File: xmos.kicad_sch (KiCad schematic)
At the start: 66 parts, among them Q1 LBSS138WT1G, Q2 BC847B, U10 SN74LVC125APWR, U7 XU316-1024-QF60B-C24, U8 W25Q128JVSIQ, U9 TLV73333PDBVR, Y2 24MHz

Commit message: routing update
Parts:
- removed R48, R49: 33R, Resistor_SMD:R_0402_1005Metric, symbol Device:R
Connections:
- net BUT_A: no longer names the net of U7.50 (X0D41)
- net XL_DN0: no longer names the net of U7.35 (X1D17)
- net XL_DN1: no longer names the net of U7.33 (X1D16)
- net XU316_WS2812: no longer names the net of U7.48 (X0D42)
- no-connect marks 1 -> 7

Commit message: routing update
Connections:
- net QSPI_D2: no longer U7.6 (X0D00)
- no-connect marks 7 -> 8
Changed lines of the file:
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@@
+	)
+	(no_connect
+		(at 52.07 48.26)
 	)
 	(no_connect
@@
 	(wire
 		(pts
-			(xy 29.21 48.26) (xy 52.07 48.26)
-		)
-		(stroke
-			(width 0)
-			(type default)
-		)
-	)
-	(wire
-		(pts
 			(xy 193.04 200.66) (xy 209.55 200.66)
 		)
@@
 		)
 	)
-	(label "QSPI_D2"
-		(at 29.21 48.26 0)
-		(effects
-			(font
-				(size 1.27 1.27)
-			)
-			(justify left bottom)
-		)
-	)

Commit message: final touches
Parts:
- D3, D4, D5, D6, D7, D8: value PESD0402-050 -> PESD0402V05
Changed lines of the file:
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@@
 			)
 		)
-		(property "Value" "PESD0402-050"
+		(property "Value" "PESD0402V05"
 			(at 195.58 180.3399 90)
 			(effects
@@
 			)
 		)
-		(property "Description" "PESD0402-050, 5V TVS, 0.3pF"
+		(property "Description" "PESD0402V05, 5V TVS, 0.3pF"
 			(at 193.04 179.07 0)
 			(effects
@@
 			)
 		)
-		(property "Value" "PESD0402-050"
+		(property "Value" "PESD0402V05"
 			(at 242.57 199.644 90)
 			(effects
@@
 			)
 		)
-		(property "Description" "PESD0402-050, 5V TVS, 0.3pF"
+		(property "Description" "PESD0402V05, 5V TVS, 0.3pF"
 			(at 250.19 204.47 0)
 			(effects
@@
 			)
 		)
-		(property "Value" "PESD0402-050"
+		(property "Value" "PESD0402V05"
 			(at 242.57 171.704 90)
 			(effects
@@
 			)
 		)
-		(property "Description" "PESD0402-050, 5V TVS, 0.3pF"
+		(property "Description" "PESD0402V05, 5V TVS, 0.3pF"
 			(at 250.19 176.53 0)
 			(effects
@@
 			)
 		)
-		(property "Value" "PESD0402-050"
+		(property "Value" "PESD0402V05"
 			(at 194.818 204.47 90)
 			(effects
@@
 			)
 		)
-		(property "Description" "PESD0402-050, 5V TVS, 0.3pF"
+		(property "Description" "PESD0402V05, 5V TVS, 0.3pF"
 			(at 193.04 204.47 0)
 			(effects
@@
 			)
 		)
-		(property "Value" "PESD0402-050"
+		(property "Value" "PESD0402V05"
 			(at 248.158 194.818 90)
 			(effects
@@
 			)
 		)
-		(property "Description" "PESD0402-050, 5V TVS, 0.3pF"
+		(property "Description" "PESD0402V05, 5V TVS, 0.3pF"
 			(at 259.08 199.39 0)
 			(effects
@@
 			)
 		)
-		(property "Value" "PESD0402-050"
+		(property "Value" "PESD0402V05"
 			(at 261.62 172.7199 90)
 			(effects
@@
 			)
 		)
-		(property "Description" "PESD0402-050, 5V TVS, 0.3pF"
+		(property "Description" "PESD0402V05, 5V TVS, 0.3pF"
 			(at 259.08 171.45 0)
 			(effects

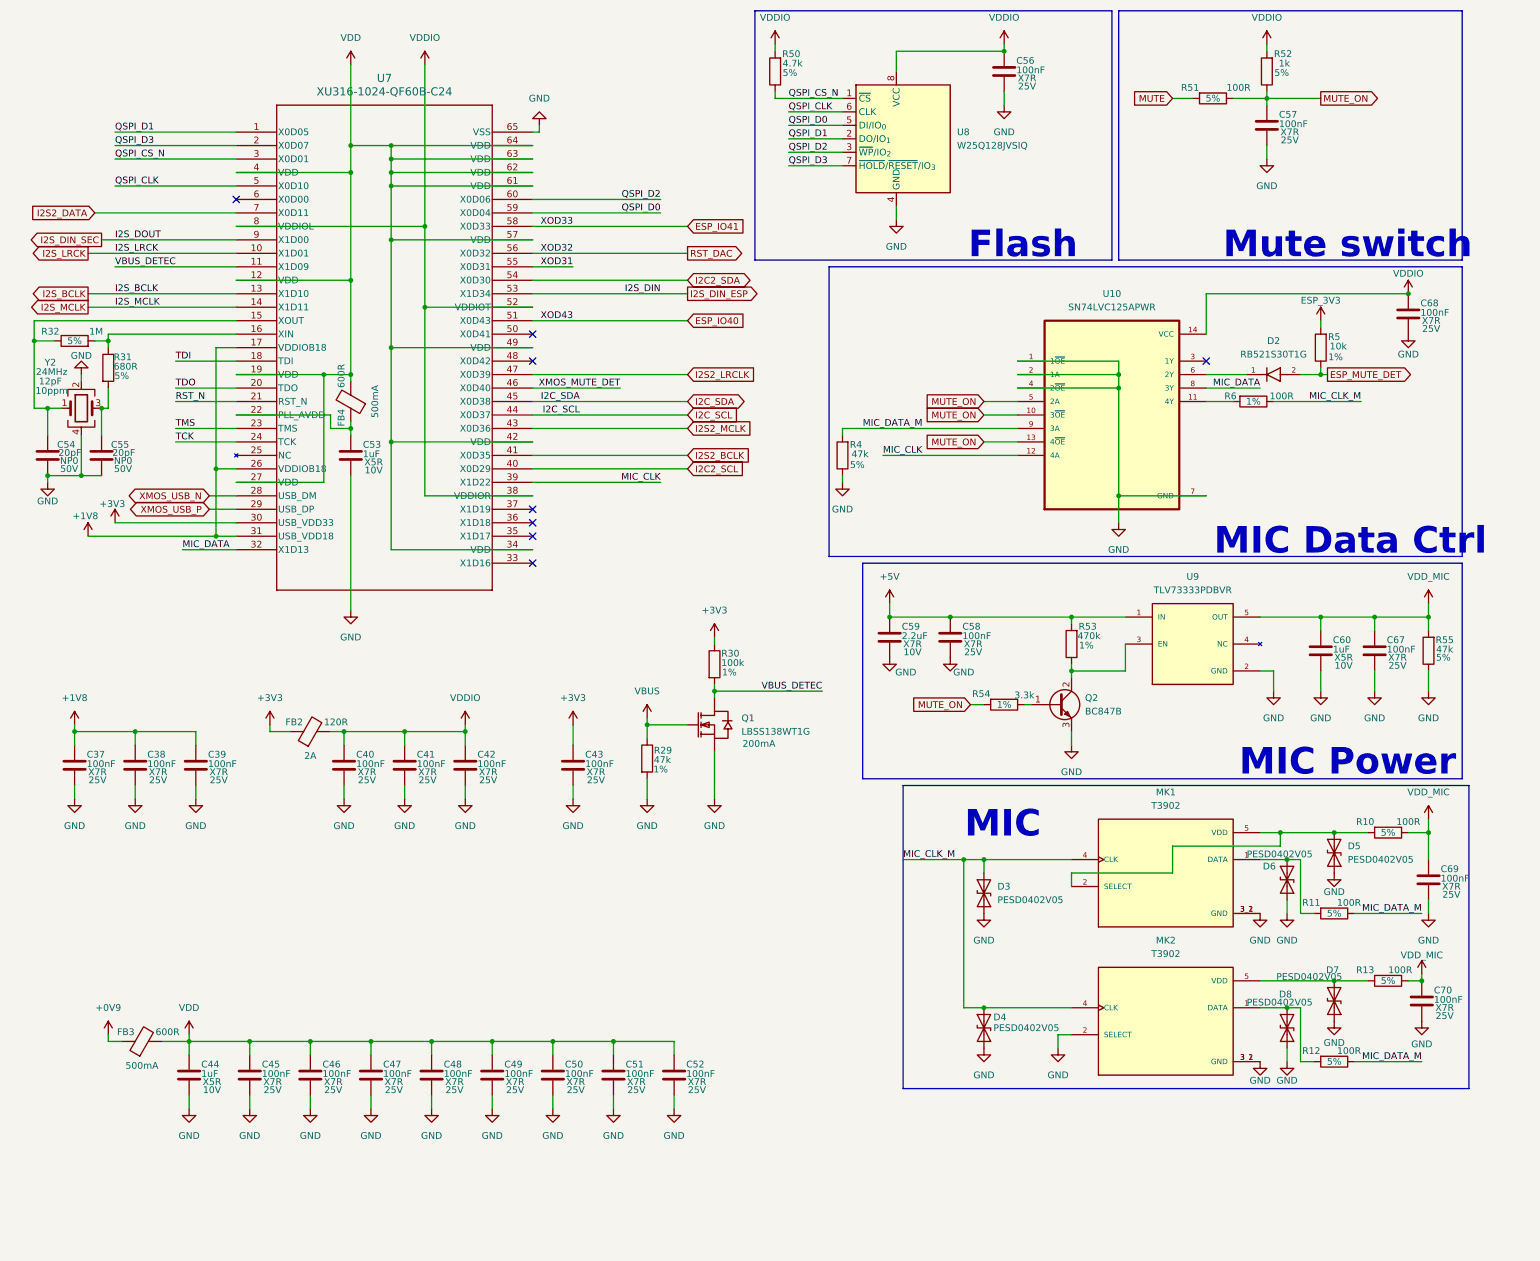
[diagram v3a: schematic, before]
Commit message: modifications for manufacturing
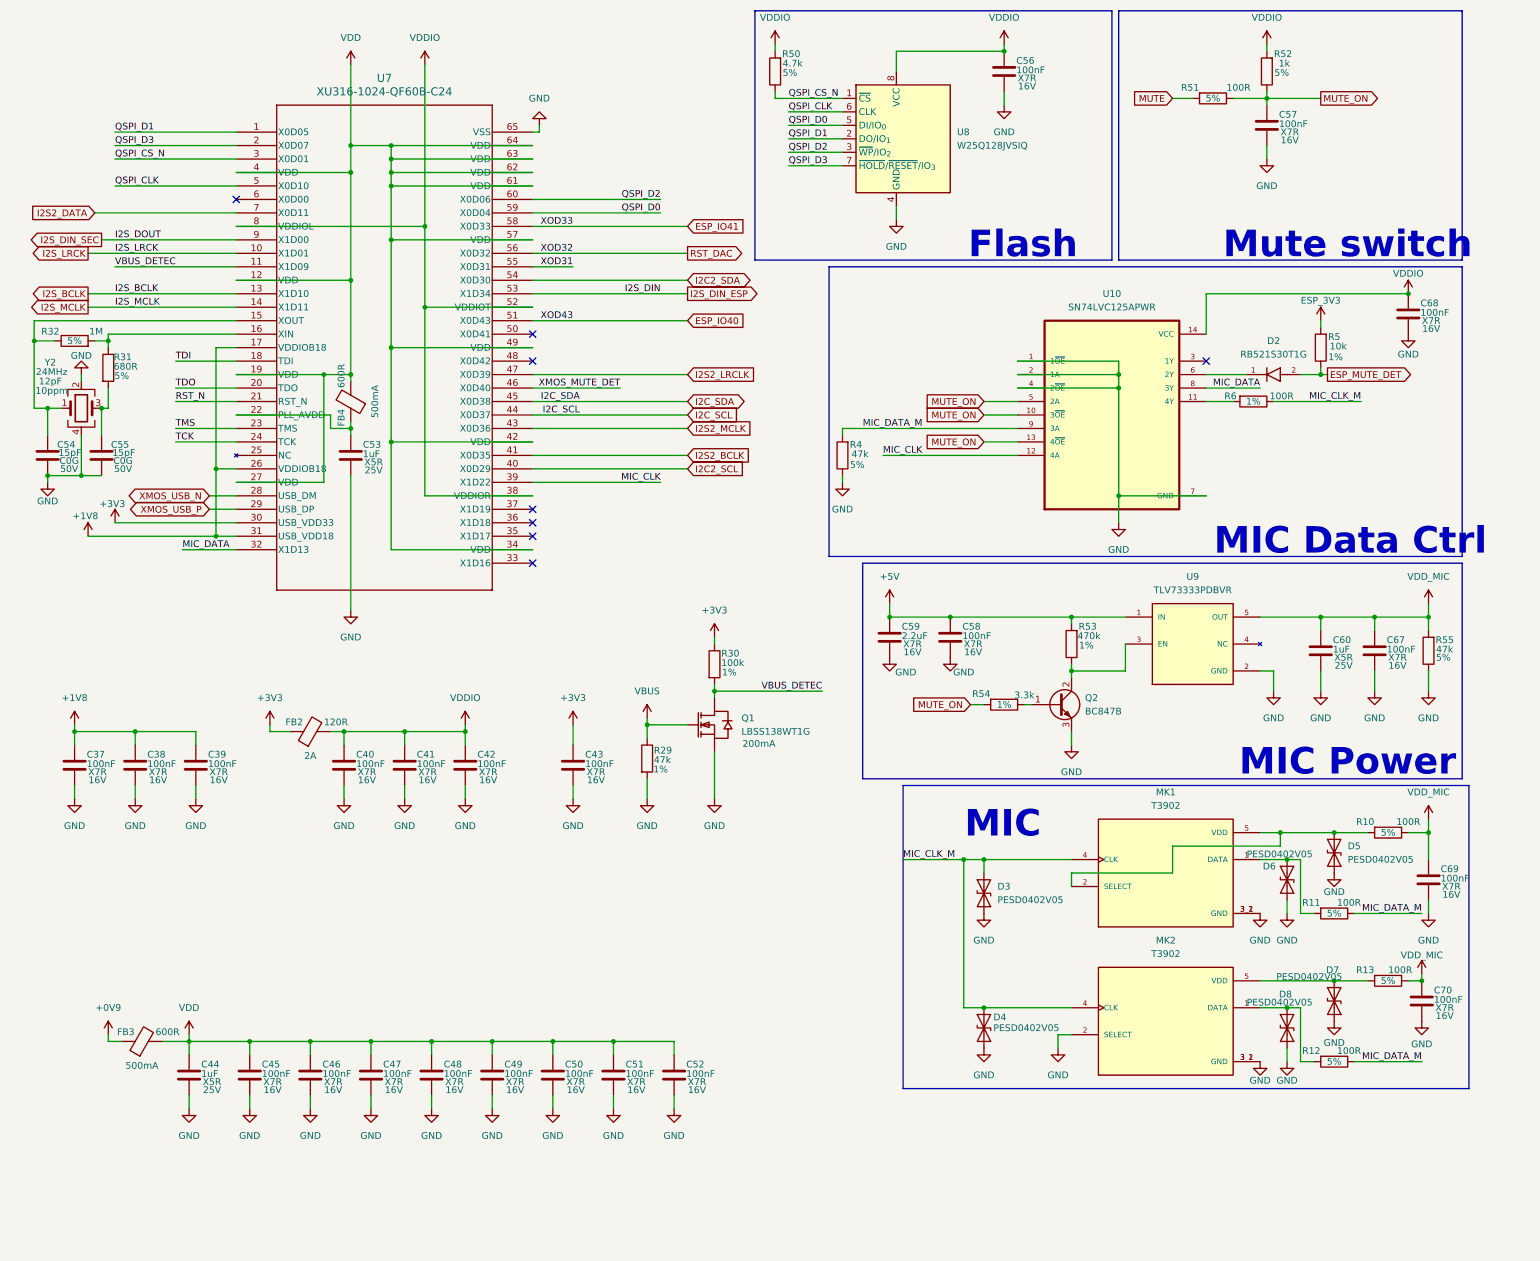
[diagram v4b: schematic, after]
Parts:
- C37, C38, C39, C40, C41, C42, C43, C45, C46, C47, C48, C49, C50, C51, C52, C56, C57, C58, C67, C68, C69, C70: Supplier Part (none) -> C1525; Voltage 25V -> 16V
- C44, C53, C60: Supplier Part (none) -> C52923; Voltage 10V -> 25V
- C54, C55: value 20pF -> 15pF; Dielectric NP0 -> C0G; Supplier Part (none) -> C1548
- C59: footprint Capacitor_SMD:C_0402_1005Metric -> Capacitor_SMD:C_0603_1608Metric; Voltage 10V -> 16V
- D2: Supplier Part (none) -> C27636108
- D3, D4, D5, D6, D7, D8: MANUFACTURER (none) -> DOWO; MP (none) -> PESD0402V05; Supplier Part (none) -> C19626254
- FB2: MANUFACTURER (none) -> Murata Electronics; MP (none) -> BLM18PG121SN1D; Supplier Part (none) -> C14709
- FB3, FB4: MANUFACTURER (none) -> Murata Electronics; MP (none) -> BLM18KG601SN1D; Part number BLM18AG601SN1D -> BLM18KG601SN1D; Supplier Part (none) -> C85833
- MK1, MK2: Supplier Part (none) -> C3171752
- Q1: MANUFACTURER (none) -> LRC; MP (none) -> LBSS138WT1G
- Q2: MANUFACTURER (none) -> hongjiacheng; MP (none) -> BC847B; Supplier Part (none) -> C20069135
- R10, R11, R12, R13, R51, R6: Supplier Part (none) -> C25076
- R29, R4, R55: Supplier Part (none) -> C25792
- R30: Supplier Part (none) -> C25530
- R31: Supplier Part (none) -> C25130
- R32: Supplier Part (none) -> C26083
- R5: Supplier Part (none) -> C25744
- R50: Supplier Part (none) -> C25900
- R52: Supplier Part (none) -> C11702
- R53: Supplier Part (none) -> C25790
- R54: Supplier Part (none) -> C25890
- U10: MANUFACTURER (none) -> Texas Instruments; Supplier Part (none) -> C7813
- U7: MANUFACTURER (none) -> XMOS; MP (none) -> XU316-1024-QF60B-C24; Supplier Part (none) -> C6617472
- U8: MANUFACTURER (none) -> Winbond Elec; MP (none) -> W25Q128JVSIQ; Supplier Part (none) -> C97521
- U9: Supplier Part (none) -> C134139
- Y2: MANUFACTURER (none) -> YXC Crystal Oscillators; MP (none) -> X322524MOB4SI; Manufacturer (none) -> YXC Crystal Oscillators; Supplier Part (none) -> C70590

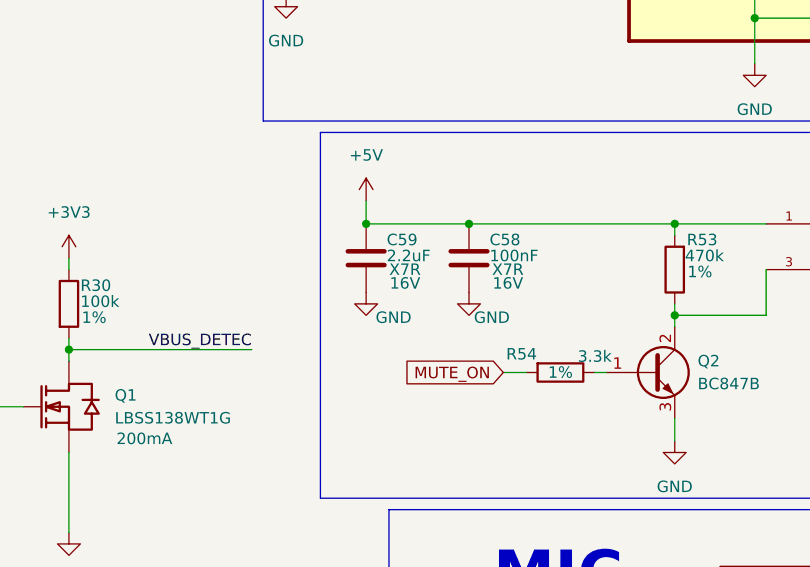
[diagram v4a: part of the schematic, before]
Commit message: modifications for manufacturing
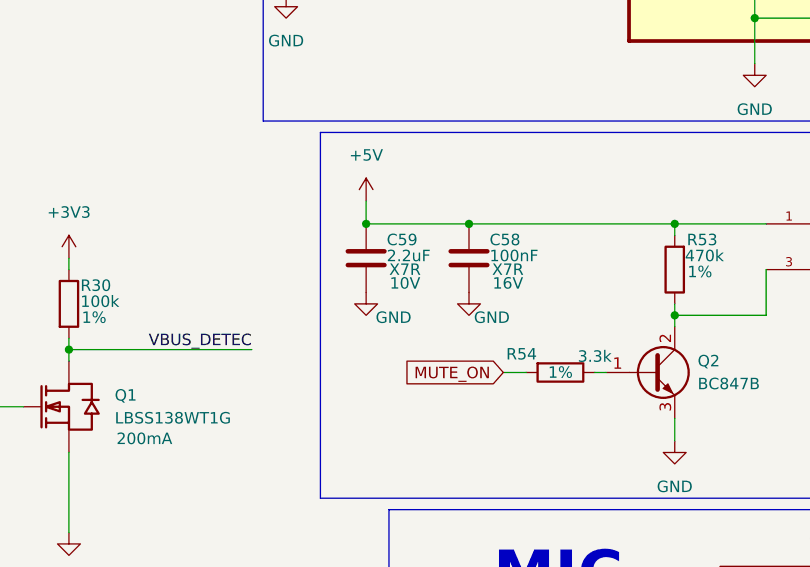
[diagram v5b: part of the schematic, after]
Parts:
- C59: Supplier Part (none) -> C86018; Voltage 16V -> 10V
- D2: Manufacturer (none) -> ON SEMICONDUCTOR; Manufacturer Part (none) -> RB521S30T1G
- D3, D4, D5, D6, D7, D8: Manufacturer (none) -> DOWO; Manufacturer Part (none) -> PESD0402V05
- FB2: Manufacturer Part (none) -> BLM18PG121SN1D
- FB3, FB4: Manufacturer Part (none) -> BLM18KG601SN1D
- MK1, MK2: Manufacturer (none) -> TDK InvenSense; Manufacturer Part (none) -> T3902
- Q2: Manufacturer (none) -> hongjiacheng; Manufacturer Part (none) -> BC847B
- U10: Manufacturer (none) -> Texas Instruments; Manufacturer Part (none) -> SN74LVC125APWR
- U7: Manufacturer (none) -> XMOS; Manufacturer Part (none) -> XU316-1024-QF60B-C24
- U8: Manufacturer (none) -> Winbond Elec; Manufacturer Part (none) -> W25Q128JVSIQ
- U9: Manufacturer (none) -> Texas Instruments; Manufacturer Part (none) -> TLV73333PDBVR
- Y2: Manufacturer Part (none) -> X322524MOB4SI

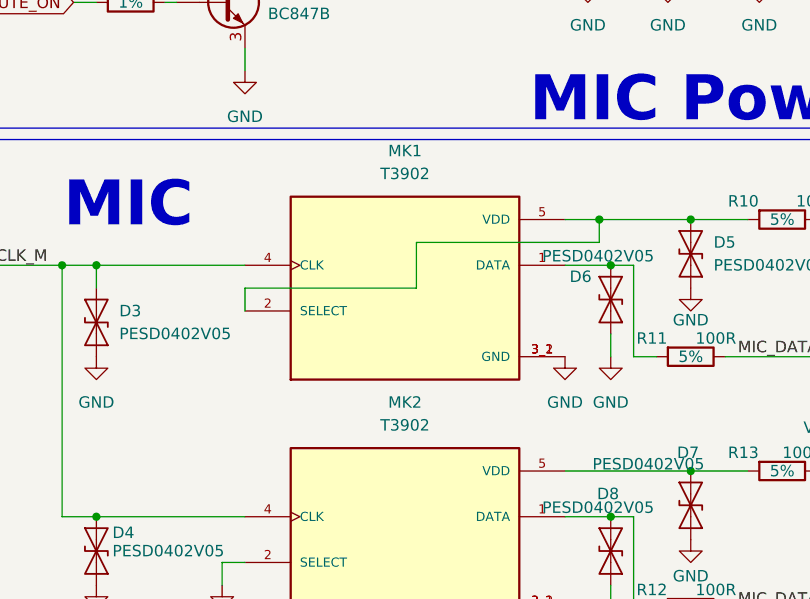
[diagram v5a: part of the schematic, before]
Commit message: modifications for manufacturing
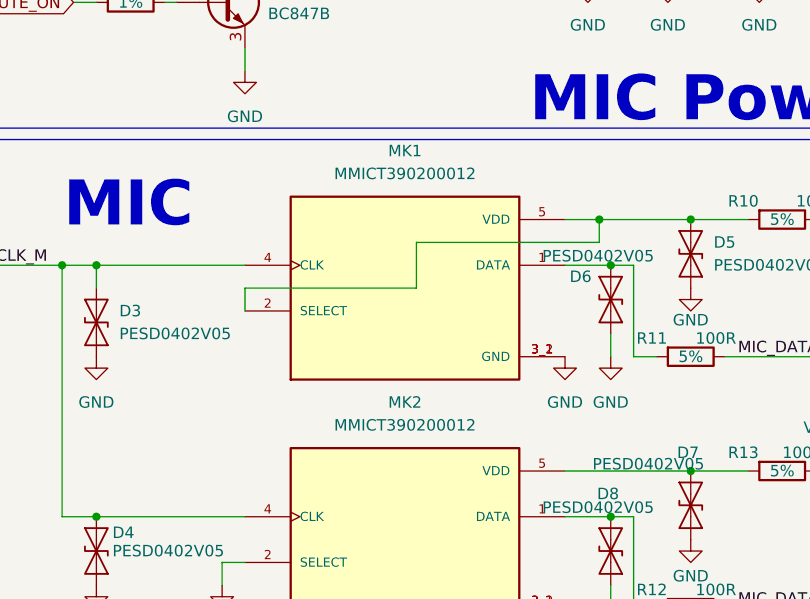
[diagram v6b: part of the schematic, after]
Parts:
- C37, C38, C39, C40, C41, C42, C43, C45, C46, C47, C48, C49, C50, C51, C52, C56, C57, C58, C67, C68, C69, C70: Manufacturer (none) -> Samsung Electro-Mechanics; Manufacturer Part (none) -> CL05B104KO5NNNC
- C44, C53, C60: Manufacturer (none) -> Samsung Electro-Mechanics; Manufacturer Part (none) -> CL05A105KA5NQNC
- C54, C55: Manufacturer (none) -> FH (Guangdong Fenghua Advanced Tech); Manufacturer Part (none) -> 0402CG150J500NT
- C59: Manufacturer (none) -> Murata Electronics; Manufacturer Part (none) -> GRM188R71A225KE15D
- MK1, MK2: value T3902 -> MMICT390200012; Manufacturer Part T3902 -> MMICT390200012
- R10, R11, R12, R13, R51, R6: Manufacturer (none) -> UNI-ROYAL(Uniroyal Elec); Manufacturer Part (none) -> 0402WGF1000TCE
- R29, R4, R55: Manufacturer (none) -> UNI-ROYAL(Uniroyal Elec); Manufacturer Part (none) -> 0402WGF4702TCE
- R30: Manufacturer (none) -> UNI-ROYAL(Uniroyal Elec); Manufacturer Part (none) -> 0402WGJ0104TCE
- R31: Manufacturer (none) -> UNI-ROYAL(Uniroyal Elec); Manufacturer Part (none) -> 0402WGF6800TCE
- R32: Manufacturer (none) -> UNI-ROYAL(Uniroyal Elec); Manufacturer Part (none) -> 0402WGF1004TCE
- R5: Manufacturer (none) -> UNI-ROYAL(Uniroyal Elec); Manufacturer Part (none) -> 0402WGF1002TCE
- R50: Manufacturer (none) -> UNI-ROYAL(Uniroyal Elec); Manufacturer Part (none) -> 0402WGF4701TCE
- R52: Manufacturer (none) -> UNI-ROYAL(Uniroyal Elec); Manufacturer Part (none) -> 0402WGF1001TCE
- R53: Manufacturer (none) -> UNI-ROYAL(Uniroyal Elec); Manufacturer Part (none) -> 0402WGF4703TCE
- R54: Manufacturer (none) -> UNI-ROYAL(Uniroyal Elec); Manufacturer Part (none) -> 0402WGF3301TCE

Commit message: modifications for manufacturing
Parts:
- C37, C38, C39, C40, C41, C42, C43, C45, C46, C47, C48, C49, C50, C51, C52, C56, C57, C58, C67, C68, C69, C70: LCSC Part # (none) -> C1525
- C44, C53, C60: LCSC Part # (none) -> C52923
- C54, C55: LCSC Part # (none) -> C1548
- C59: LCSC Part # (none) -> C86018
- D2: LCSC Part # (none) -> C27636108
- D3, D4, D5, D6, D7, D8: LCSC Part # (none) -> C19626254
- FB2: LCSC Part # (none) -> C14709
- FB3, FB4: LCSC Part # (none) -> C85833
- MK1, MK2: LCSC Part # (none) -> C3171752
- Q1: LCSC Part # (none) -> C383201
- Q2: LCSC Part # (none) -> C20069135
- R10, R11, R12, R13, R51, R6: LCSC Part # (none) -> C25076
- R29, R4, R55: LCSC Part # (none) -> C25792
- R30: LCSC Part # (none) -> C25530
- R31: LCSC Part # (none) -> C25130
- R32: LCSC Part # (none) -> C26083
- R5: LCSC Part # (none) -> C25744
- R50: LCSC Part # (none) -> C25900
- R52: LCSC Part # (none) -> C11702
- R53: LCSC Part # (none) -> C25790
- R54: LCSC Part # (none) -> C25890
- U10: LCSC Part # (none) -> C7813
- U7: LCSC Part # (none) -> C6617472
- U8: LCSC Part # (none) -> C97521
- U9: LCSC Part # (none) -> C134139
- Y2: LCSC Part # (none) -> C70590

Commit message: rev2 update
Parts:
- added C92: 100nF, Capacitor_SMD:C_0402_1005Metric, symbol Seeed_libadl:Capacitors/302010024
- added Q3: LBSS138WT1G, Package_TO_SOT_SMD:SOT-323_SC-70, symbol Seeed_libadl:Mosfet/305031542
- added R33: 470K, Resistor_SMD:R_0402_1005Metric, symbol Seeed_libdb:Resistors/301010069
- added R34: 10K, Resistor_SMD:R_0402_1005Metric, symbol Seeed_libadl:Resistors/301010047
- added R63: 100R, Resistor_SMD:R_0402_1005Metric, symbol Seeed_libadl:Resistors/301010028
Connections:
- net +1V8: now also R34.2
- net GND: now also C92.2, Q3.2 (S), R33.1
- net RST_N: now also C92.1, Q3.3 (D), R34.1
- new net: Q3.1 (G), R33.2, R63.1
- new net XU316_RST: R63.2
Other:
- moved on the sheet: C37, C38, C39, C40, C41, C42, C43, C44, C45, C46, C47, C48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
